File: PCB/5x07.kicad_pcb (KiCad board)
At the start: 2 copper layers, 165.9 x 100.8 mm, 127 parts, among them J1 AVR-ISP-6, K0 KC_ESC, K1 KC_GRV, K10 SW_Push, K11 KC_TAB, K12 KC_Q, K13 KC_W, K14 KC_E, K15 KC_R, K16 KC_T, K2 KC_1, K20 SW_Push, K21 KC_CAPS, K22 KC_A, K23 KC_S, K24 KC_D, K25 KC_F, K26 KC_G, K3 KC_2, K30 SW_Push, K31 KC_LSFT, K32 KC_Z, K33 KC_X, K34 KC_C, K35 KC_V, K36 KC_B, K4 KC_3, K40 SW_Push, K41 KC_LCTL, K42 KC_LGUI, K43 KC_LALT, K44 KC_FN, K45 KC_SPACE, K46 KC_SPACE, K5 KC_4, K6 KC_5, SW1 SW_Push, U1 ATmega32U4-A, U2 PRTR5V0U2X, Y1 16MHz

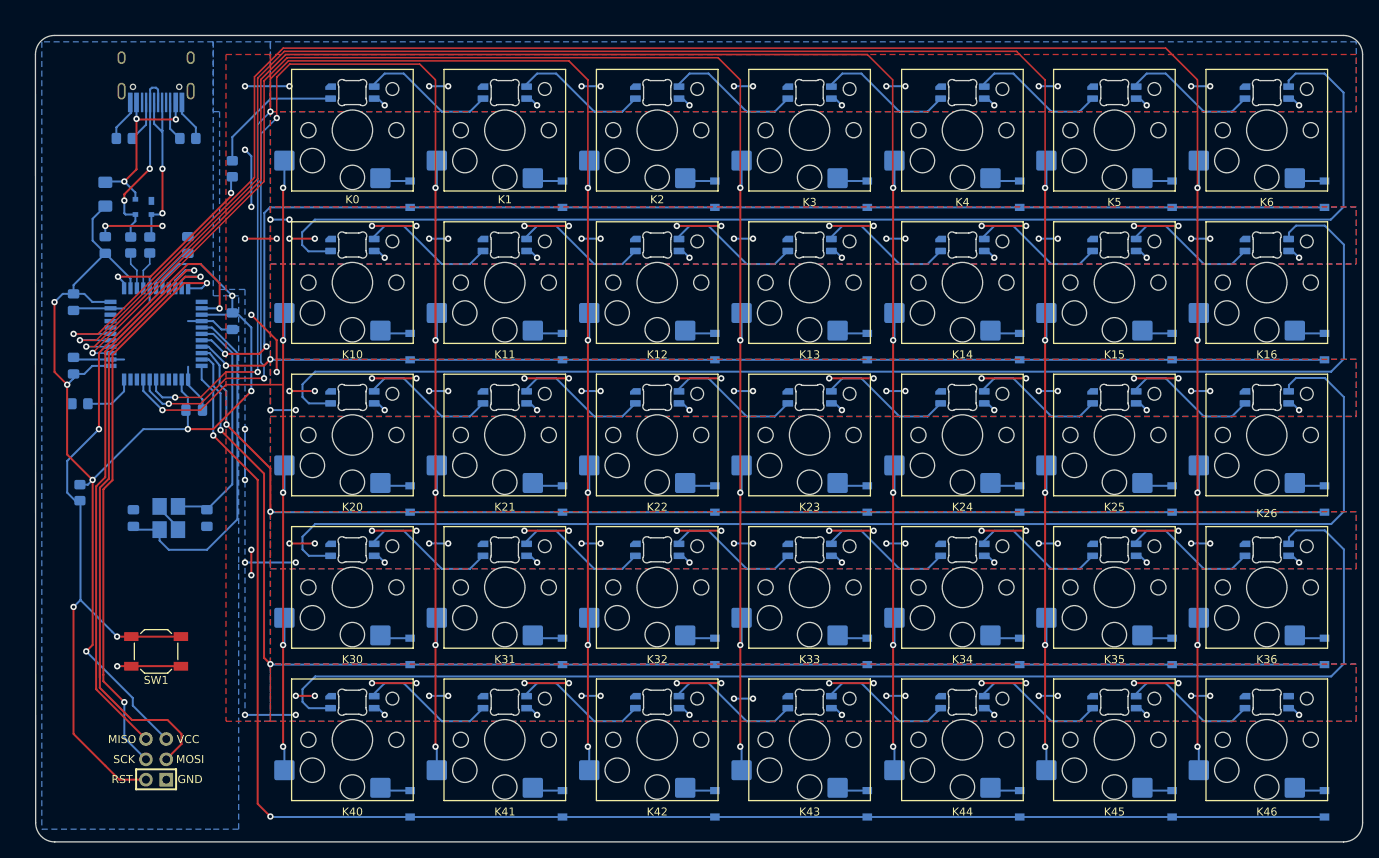
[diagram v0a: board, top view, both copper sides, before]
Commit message: v2: reversiblility for LHS and RHS
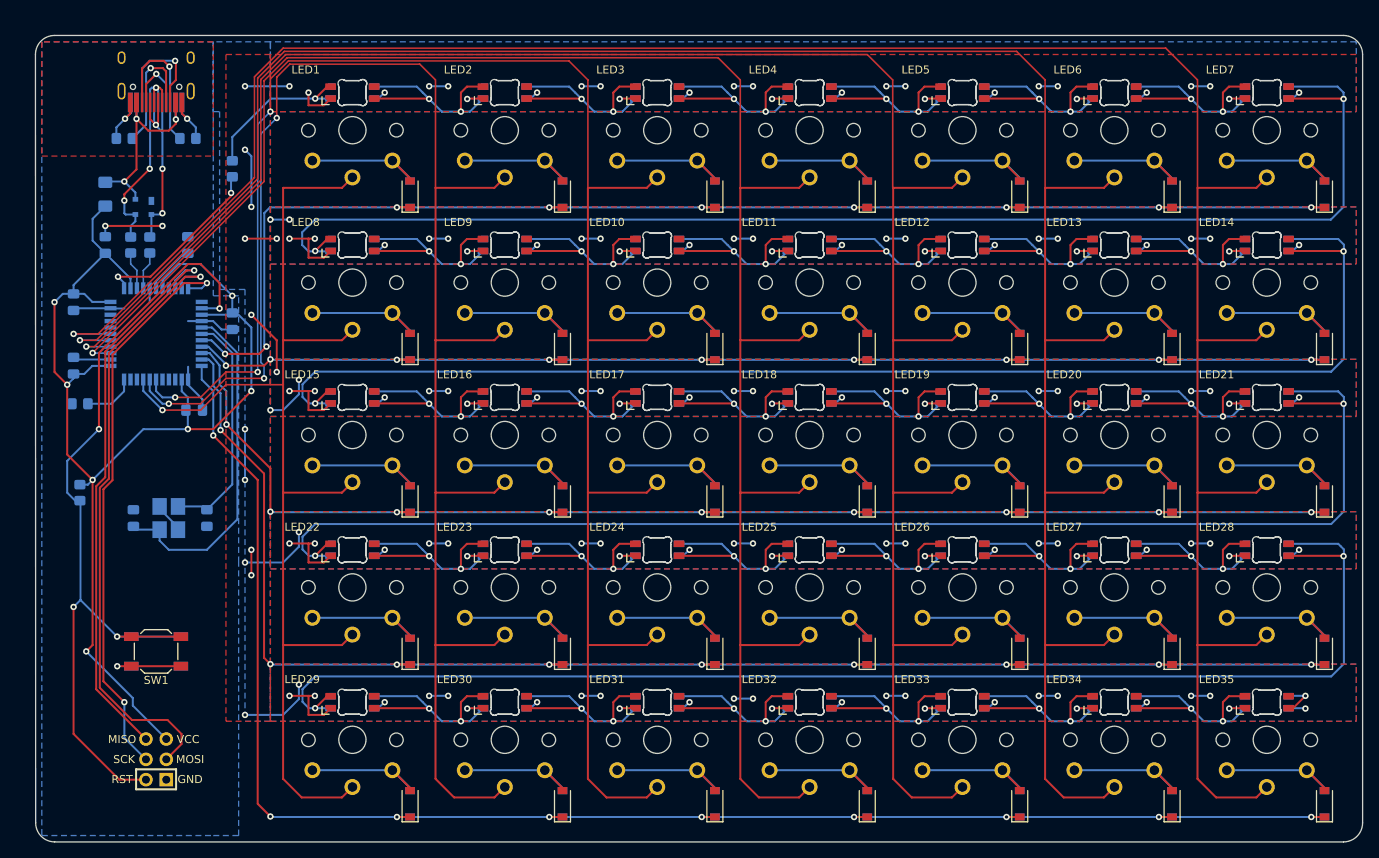
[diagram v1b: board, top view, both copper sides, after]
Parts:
- D0, D1, D10, D11, D12, D13, D14, D15, D16, D2, D20, D21, D22, D23, D24, D25, D26, D3, D30, D31, D32, D33, D34, D35, D36, D4, D40, D41, D42, D43, D44, D45, D46, D5, D6: footprint Diode_SMD:D_SOD-123 -> assets:D_SOD-123-Reversible
- K0, K1, K10, K11, K12, K13, K14, K15, K16, K2, K20, K21, K22, K23, K24, K25, K26, K3, K30, K31, K32, K33, K34, K35, K36, K4, K40, K41, K42, K43, K44, K45, K46, K5, K6: footprint Switch_Keyboard_Hotswap_Kailh:SW_Hotswap_Kailh_Choc_V1V2_1.00u -> assets:SW_choc_1u_reversible
- LED1, LED10, LED11, LED12, LED13, LED14, LED15, LED16, LED17, LED18, LED19, LED2, LED20, LED21, LED22, LED23, LED24, LED25, LED26, LED27, LED28, LED29, LED3, LED30, LED31, LED32, LED33, LED34, LED35, LED4, LED5, LED6, LED7, LED8, LED9: footprint marbastlib-choc:LED_choc_6028R -> assets:LED_choc_6028R_Reversible_same_side
- SW1: footprint Button_Switch_SMD:SW_SPST_SKQG_WithStem -> assets:SW_SPST_SKQG_WithStem_Reversible
- USB1: footprint Type-C:HRO-TYPE-C-31-M-12-HandSoldering -> assets:HRO-TYPE-C-31-M-12-HandSoldering-Reversible
- turned K0 to 0 degrees
- turned K1 to 0 degrees
- turned K10 to 0 degrees
- turned K11 to 0 degrees
- turned K12 to 0 degrees
- turned K13 to 0 degrees
- turned K14 to 0 degrees
- turned K15 to 0 degrees
- turned K16 to 0 degrees
- turned K2 to 0 degrees
- turned K20 to 0 degrees
- turned K21 to 0 degrees
- turned K22 to 0 degrees
- turned K23 to 0 degrees
- turned K24 to 0 degrees
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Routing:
- net GND: track 218.4 -> 171.8 mm, vias 65 -> 50
- net col4: track 226.8 -> 262.0 mm, vias 6 -> 1
- net col5: track 247.4 -> 282.6 mm, vias 6 -> 1
- net col3: track 206.1 -> 241.4 mm, vias 6 -> 1
- net col1: track 176.8 -> 212.0 mm, vias 8 -> 3
- net col2: track 193.8 -> 229.0 mm, vias 8 -> 3
- net col6: track 268.3 -> 303.3 mm, vias 6 -> 1
- net col0: track 107.1 -> 142.1 mm, vias 6 -> 1
- net unconnected-(USB1-Pad3): track 0.00 -> 14.3 mm, vias 0 -> 1
- net Net-(D0-Pad2): track 3.36 -> 16.6 mm
- net Net-(D36-Pad2): track 3.36 -> 16.6 mm
- net Net-(D24-Pad2): track 3.31 -> 16.3 mm
- net Net-(D14-Pad2): track 3.31 -> 16.3 mm
- net Net-(D4-Pad2): track 3.31 -> 16.3 mm
- net Net-(D44-Pad2): track 3.31 -> 16.3 mm
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- added copper zone on F.Cu, net GND
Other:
- board text added: "GND"
- board text added: "MISO"
- board text added: "MOSI"
- board text added: "RST"
- board text added: "SCK"
- board text added: "VCC"

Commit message: v3: TRRS for split sides
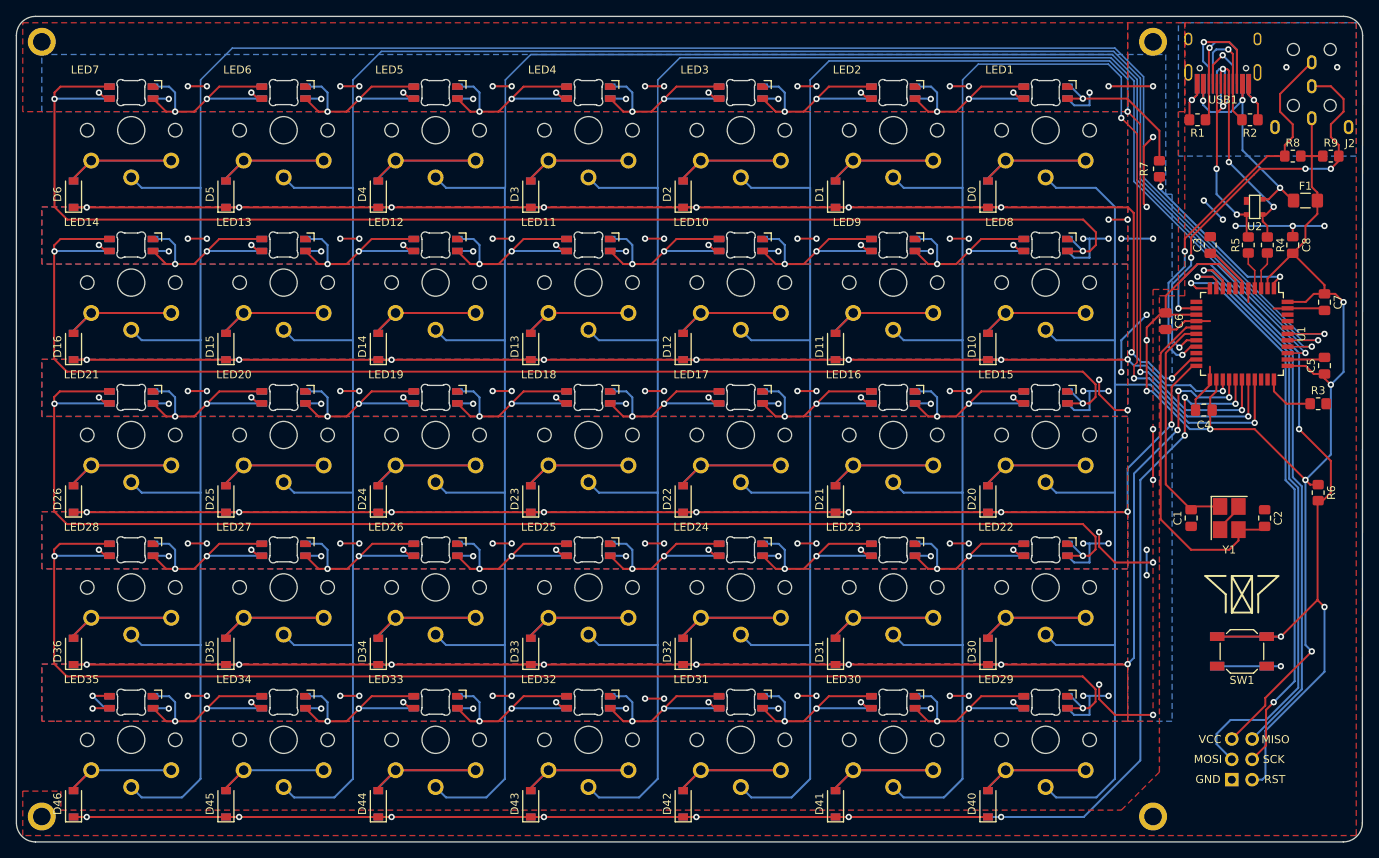
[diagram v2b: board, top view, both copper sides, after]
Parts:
- added H1: MountingHole_Pad, random-keyboard-parts:Generic-Mounthole, F.Cu at (55.6, 33.3)
- added H2: MountingHole_Pad, random-keyboard-parts:Generic-Mounthole, F.Cu at (194.5, 33.3)
- added H3: MountingHole_Pad, random-keyboard-parts:Generic-Mounthole, F.Cu at (55.6, 130.2)
- added H4: MountingHole_Pad, random-keyboard-parts:Generic-Mounthole, F.Cu at (194.5, 130.2)
- added J2: AudioJack3_Ground, assets:PJ-3200B-4A-Reversible, F.Cu at (214.3, 32.7)
- added R8: 3.3k, Resistor_SMD:R_0805_2012Metric_Pad1.20x1.40mm_HandSolder, F.Cu at (211.9, 47.6)
- added R9: 3.3k, Resistor_SMD:R_0805_2012Metric_Pad1.20x1.40mm_HandSolder, F.Cu at (216.7, 47.6)
- added REF**: 5x07, assets:5x07, F.Cu at (205.6, 102.4)
- C1, C2, C3, C4, C5, C6, C7, C8, D0, D1, D10, D11, D12, D13, D14, D15, D16, D2, D20, D21, D22, D23, D24, D25, D26, D3, D30, D31, D32, D33, D34, D35, D36, D4, D40, D41, D42, D43, D44, D45, D46, D5, D6, F1, LED1, LED10, LED11, LED12, LED13, LED14, LED15, LED16, LED17, LED18, LED19, LED2, LED20, LED21, LED22, LED23, LED24, LED25, LED26, LED27, LED28, LED29, LED3, LED30, LED31, LED32, LED33, LED34, LED35, LED4, LED5, LED6, LED7, LED8, LED9, R1, R2, R3, R4, R5, R6, R7, U1, U2, USB1, Y1: moved to F.Cu
- J1, K0, K1, K10, K11, K12, K13, K14, K15, K16, K2, K20, K21, K22, K23, K24, K25, K26, K3, K30, K31, K32, K33, K34, K35, K36, K4, K40, K41, K42, K43, K44, K45, K46, K5, K6, SW1: moved to B.Cu
- moved C5 156.4 mm to (215.9, 73.8)
- moved C7 156.4 mm to (215.9, 65.9)
- moved D16 156.4 mm to (59.5, 71.4)
- moved D26 156.4 mm to (59.5, 90.5)
- moved D36 156.4 mm to (59.5, 109.5)
- moved D46 156.4 mm to (59.5, 128.6)
- moved D6 156.4 mm to (59.5, 52.4)
- moved R3 154.8 mm to (215.1, 78.6), turned to 0 degrees
- moved R6 154.8 mm to (215.1, 89.7)
- moved F1 150.0 mm to (213.5, 53.2), turned to 0 degrees
- moved C8 148.4 mm to (211.9, 58.7)
- moved R4 142.1 mm to (208.8, 58.7)
- moved K16 141.9 mm to (66.7, 63.4), turned to 180 degrees
- moved K26 141.9 mm to (66.7, 82.5), turned to 180 degrees
- moved K36 141.9 mm to (66.7, 101.5), turned to 180 degrees
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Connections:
- U1 pad 18: row0 -> SCL
- U1 pad 19: row1 -> SDA
- U1 pad 20: row2 -> unconnected-(U1-Pad20)
- U1 pad 21: row3 -> row0
- U1 pad 22: row4 -> row2
- U1 pad 25: unconnected-(U1-Pad25) -> row1
- U1 pad 26: unconnected-(U1-Pad26) -> row3
- U1 pad 27: unconnected-(U1-Pad27) -> row4
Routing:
- net SCL: track 0.00 -> 53.4 mm, vias 0 -> 4
- net SDA: track 0.00 -> 49.9 mm, vias 0 -> 2
- net +5V: track 314.5 -> 330.4 mm
- net Net-(D3-Pad2): track 16.3 -> 26.3 mm
- net Net-(D23-Pad2): track 16.3 -> 26.3 mm
- net Net-(D13-Pad2): track 16.3 -> 26.3 mm
- net Net-(D43-Pad2): track 16.3 -> 26.3 mm
- net Net-(D33-Pad2): track 16.3 -> 26.3 mm
- net Net-(D6-Pad2): track 16.3 -> 26.3 mm
- net Net-(D24-Pad2): track 16.3 -> 26.3 mm
- net Net-(D21-Pad2): track 16.3 -> 26.3 mm
- net Net-(D14-Pad2): track 16.3 -> 26.3 mm
- net Net-(D41-Pad2): track 16.3 -> 26.3 mm
- net Net-(D36-Pad2): track 16.6 -> 26.6 mm
- net Net-(D32-Pad2): track 16.3 -> 26.3 mm
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- added copper zone on B.Cu, net +5V
- removed copper zone on F.Cu, net +5V
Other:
- board size 165.9 x 100.8 mm -> 168.3 x 103.2 mm

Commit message: bugfix
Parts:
- J1: footprint random-keyboard-parts:Reset_Pretty-Mask -> random-keyboard-parts:Reset_Pretty
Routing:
- net row4: track 203.6 -> 205.2 mm
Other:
- board text added: "5x07 v3"
- board text added: "Zokhoi 2022"

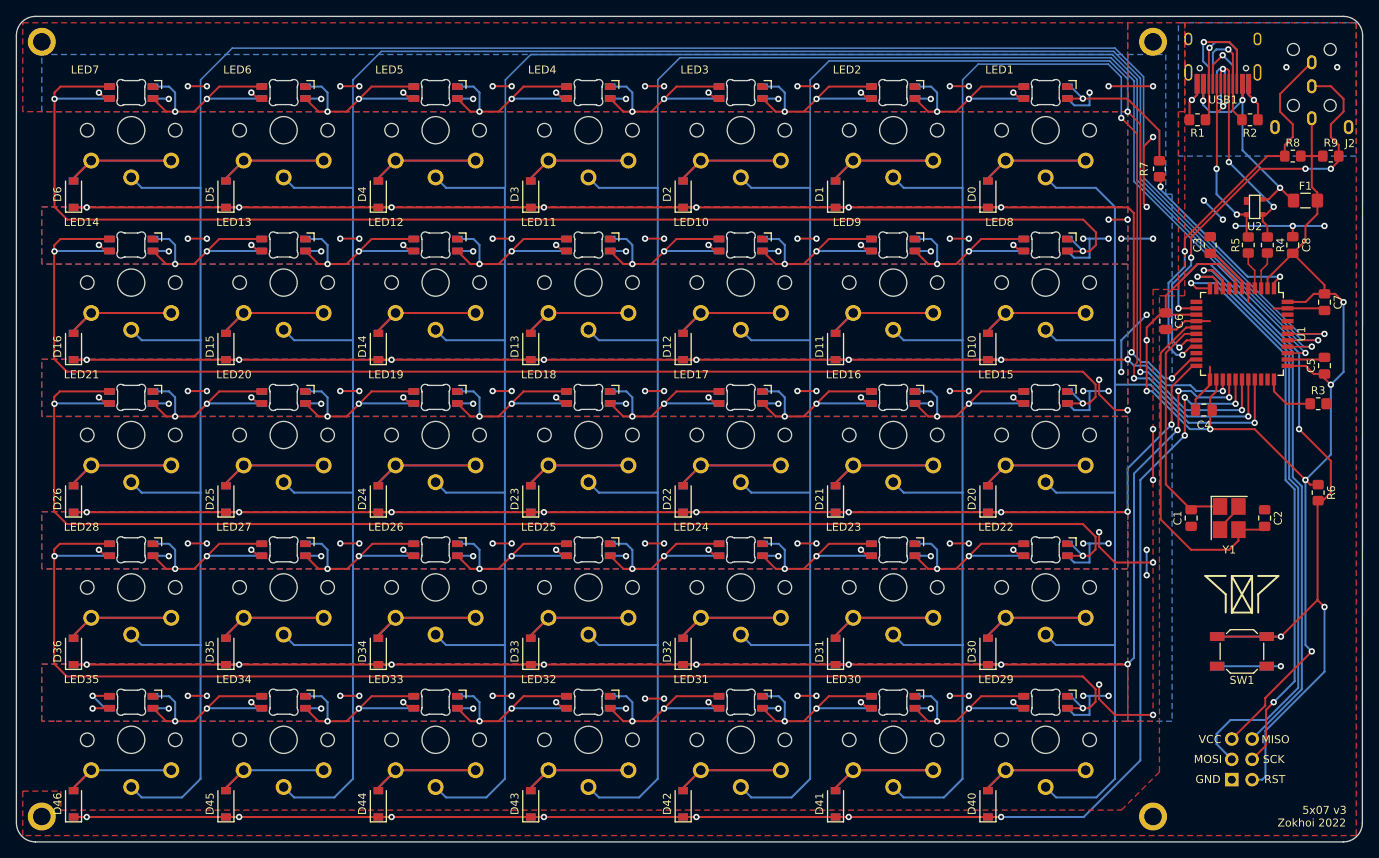
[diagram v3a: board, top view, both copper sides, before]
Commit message: minified TRRS jack footprint and other bugfixes
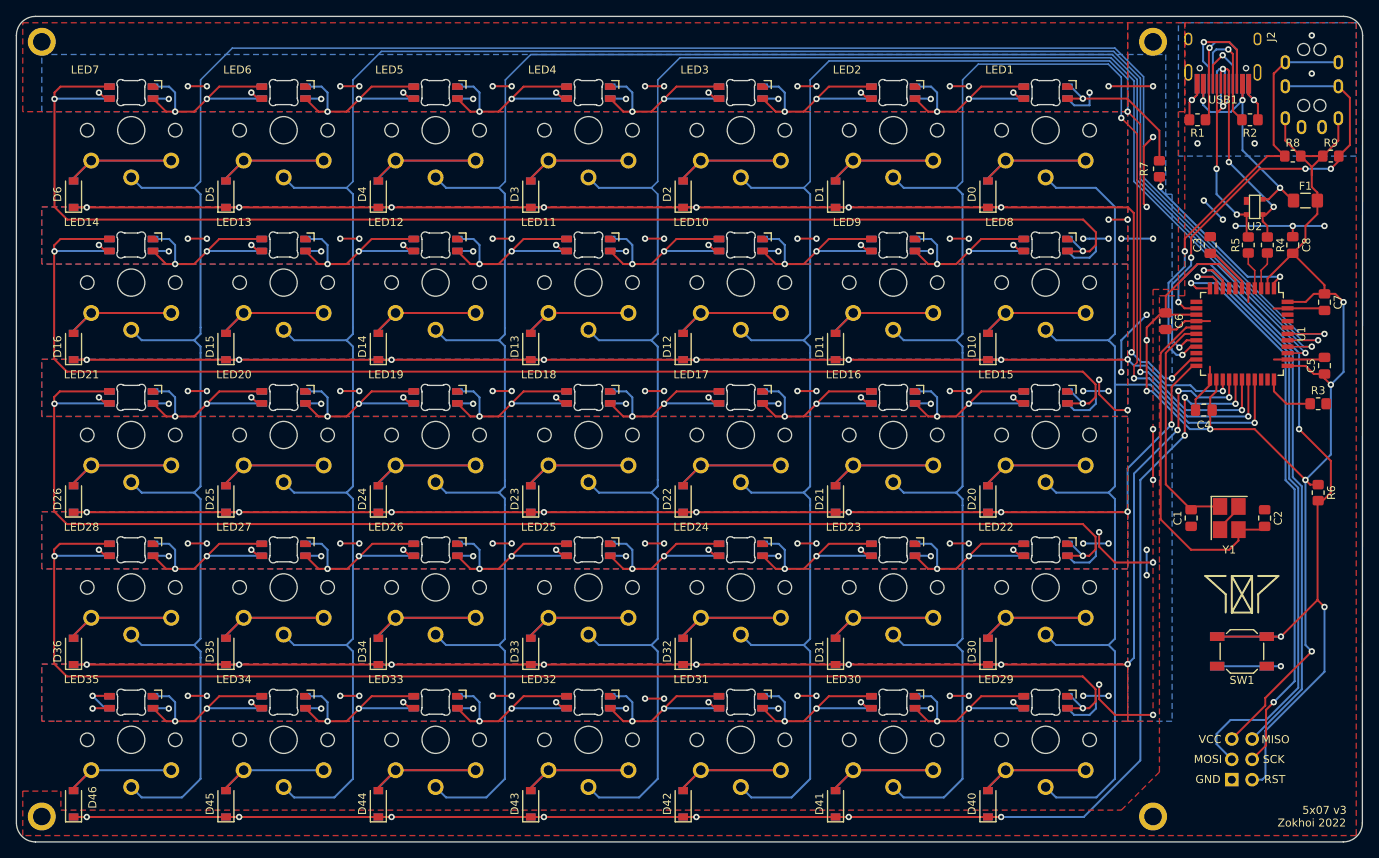
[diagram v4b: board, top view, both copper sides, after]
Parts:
- J2: footprint assets:PJ-3200B-4A-Reversible -> assets:PJ-3200B-4A-Reversible-Mini
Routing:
- net +5V: track 330.4 -> 340.6 mm
- net SDA: track 49.9 -> 55.0 mm
- net SCL: track 53.4 -> 57.1 mm
- net GND: track 178.5 -> 181.6 mm, vias 55 -> 57
- net col6: track 303.3 -> 302.7 mm
- net col5: track 282.6 -> 282.1 mm
- net col3: track 241.4 -> 240.8 mm
- net col1: track 215.2 -> 214.7 mm
- net col2: track 231.7 -> 231.2 mm

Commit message: added build pics and instructions
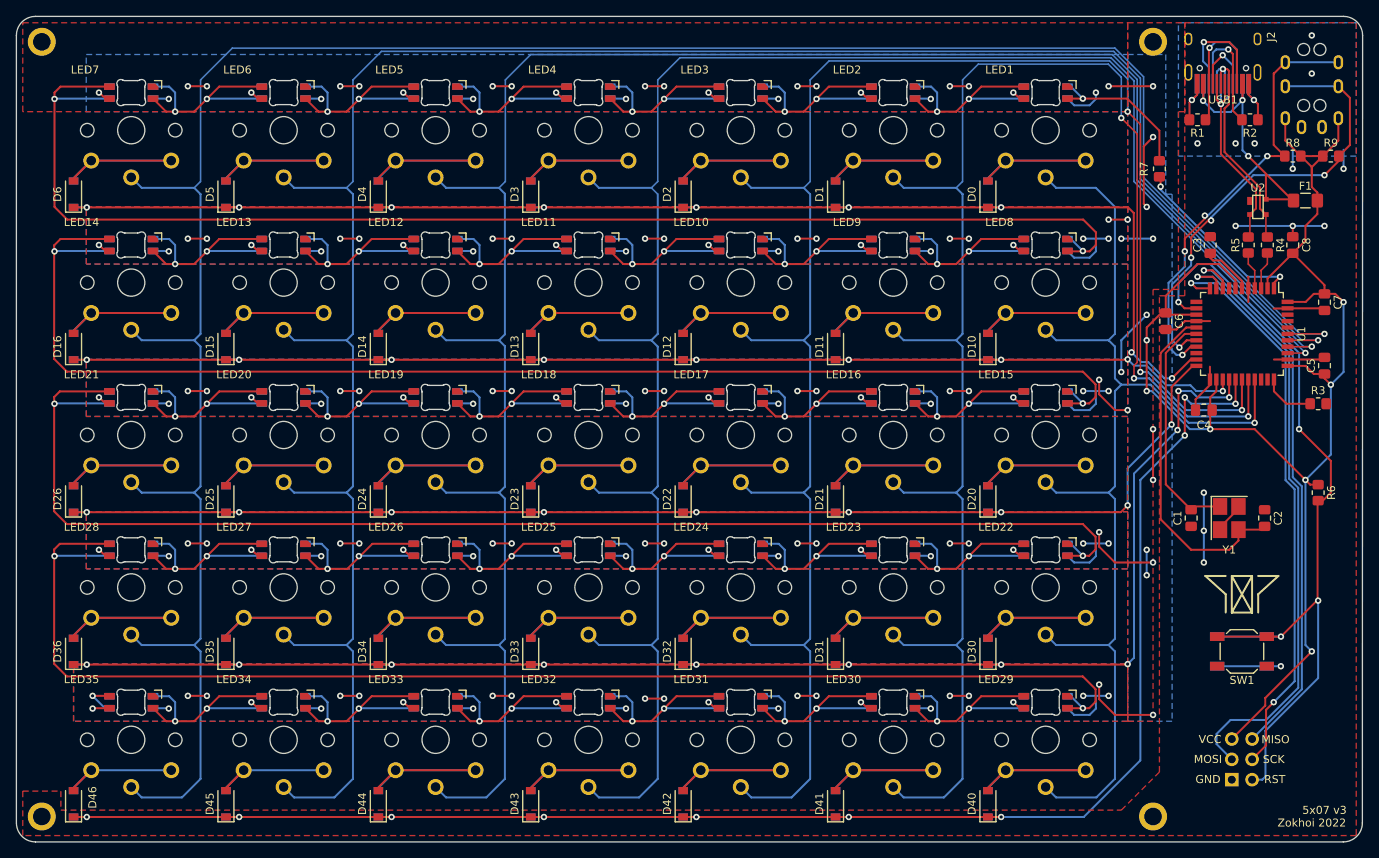
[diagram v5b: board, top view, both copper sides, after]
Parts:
- R8, R9: value 3.3k -> 10k
- moved U2 0.41 mm to (207.6, 54.0)
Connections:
- net Net-(R4-Pad1) renamed /D_N
- net Net-(R5-Pad1) renamed /D_P
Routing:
- net GND: track 181.6 -> 193.5 mm, vias 57 -> 61
- net VCC: track 32.8 -> 36.8 mm
- net /D_P: track 31.4 -> 29.8 mm, vias 3 -> 1
- net /D_N: track 31.3 -> 30.4 mm, vias 3 -> 1
- net Net-(C3-Pad2): track 5.82 -> 6.62 mm
- net RESET: track 108.8 -> 108.0 mm
- net SDA: track 55.0 -> 55.3 mm, vias 2 -> 4
